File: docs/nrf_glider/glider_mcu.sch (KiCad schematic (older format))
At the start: 8 parts, among them J1 PROG, J2 Conn_01x06_Male, J3 Conn_01x06_Male, U1 MSP430G2553IPW20, U2 25LC640, U3 NRF24L01_Breakout

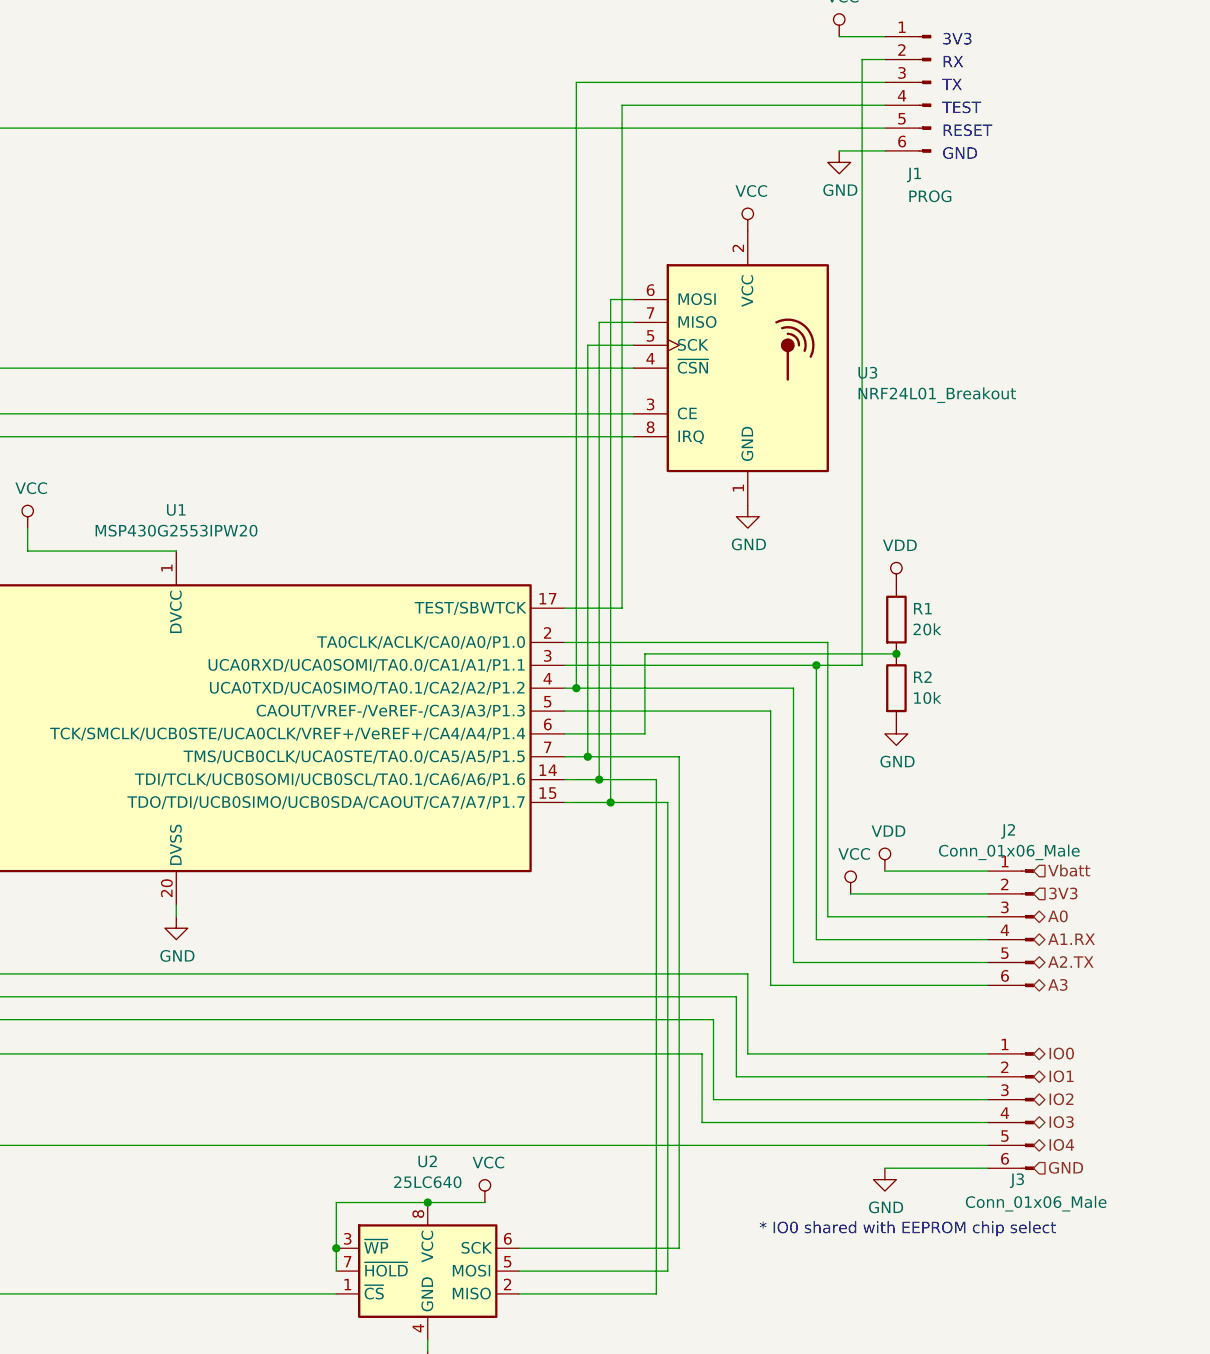
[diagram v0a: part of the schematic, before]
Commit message: Rerouted Rx module for center buzzer
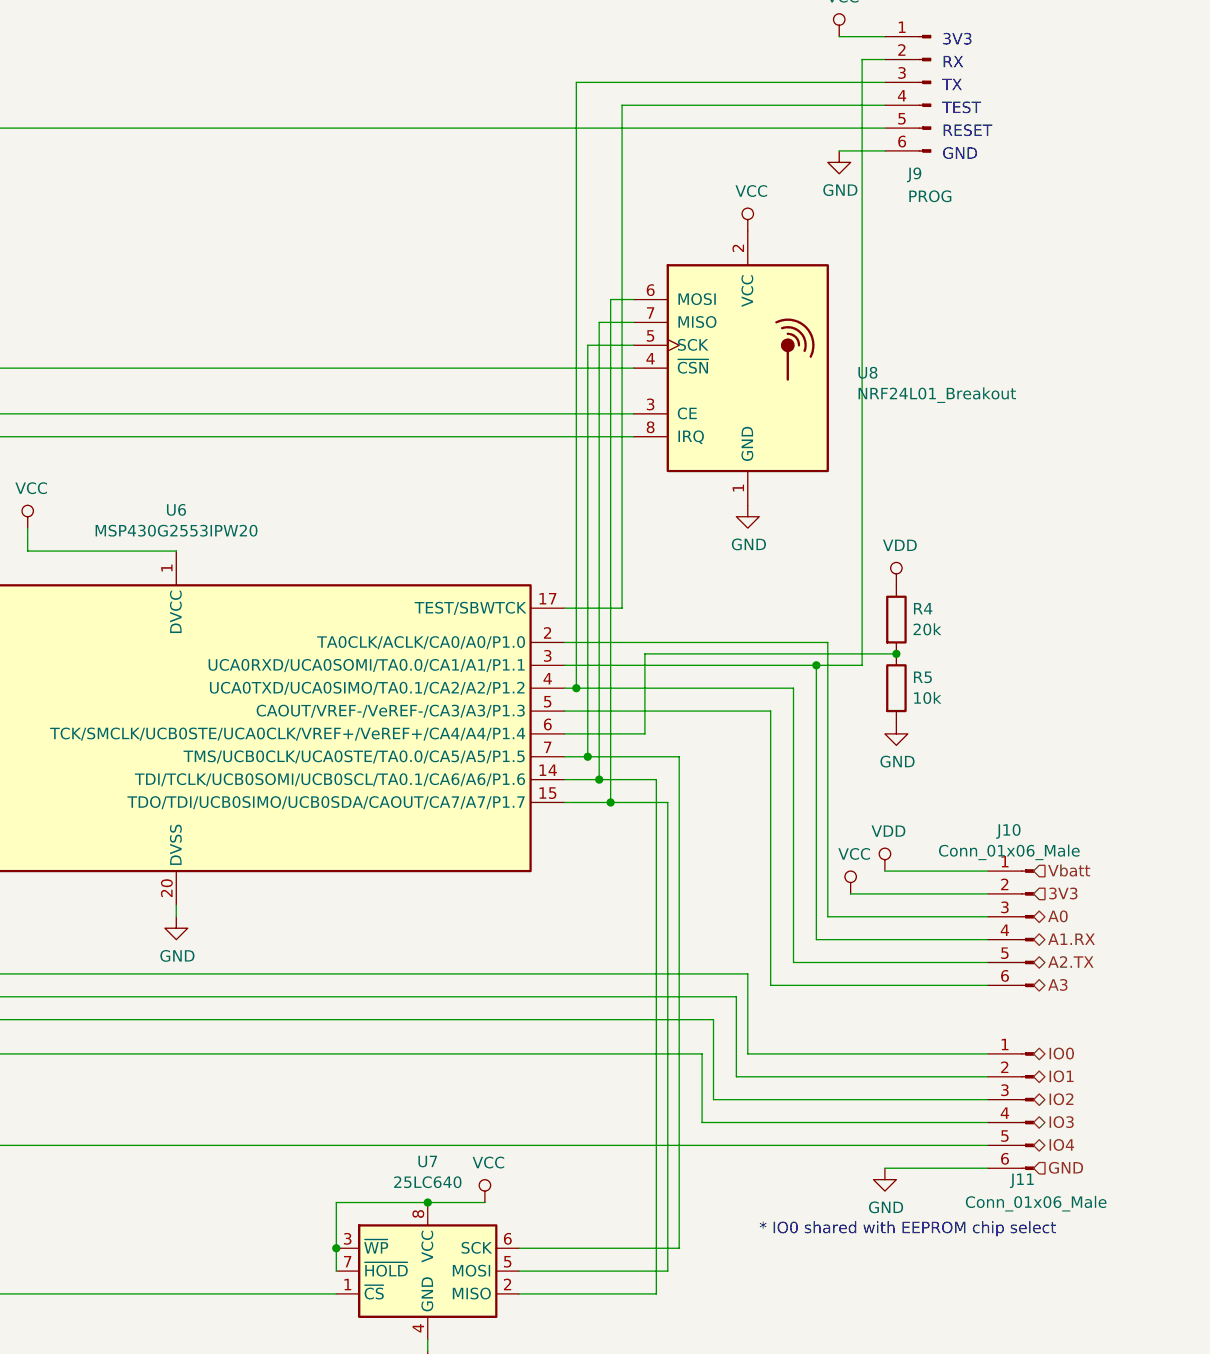
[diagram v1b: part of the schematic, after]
